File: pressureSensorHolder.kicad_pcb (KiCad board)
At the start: 2 copper layers, 65 x 61.1 mm, 12 parts, among them J1 Conn_01x04, U1 SDP8xx-ANALOG

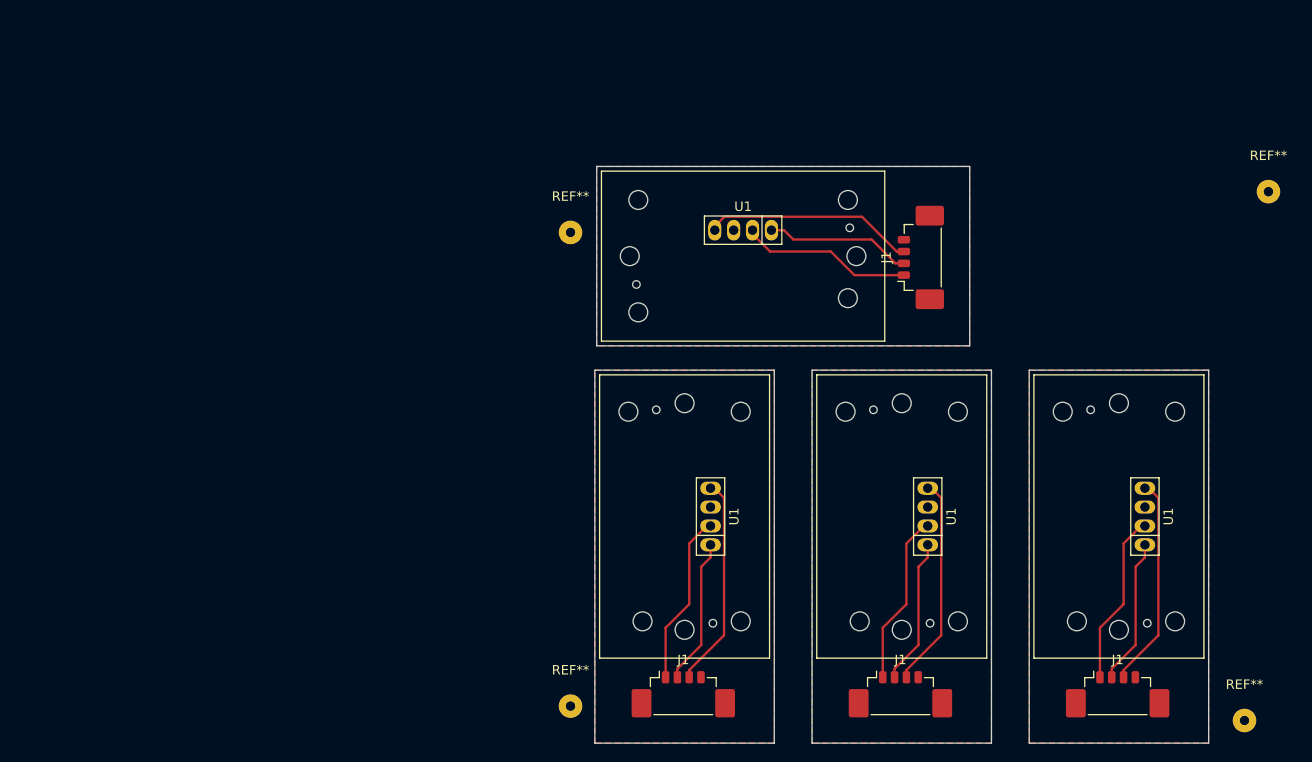
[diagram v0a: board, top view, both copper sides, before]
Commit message: Corrected sizes
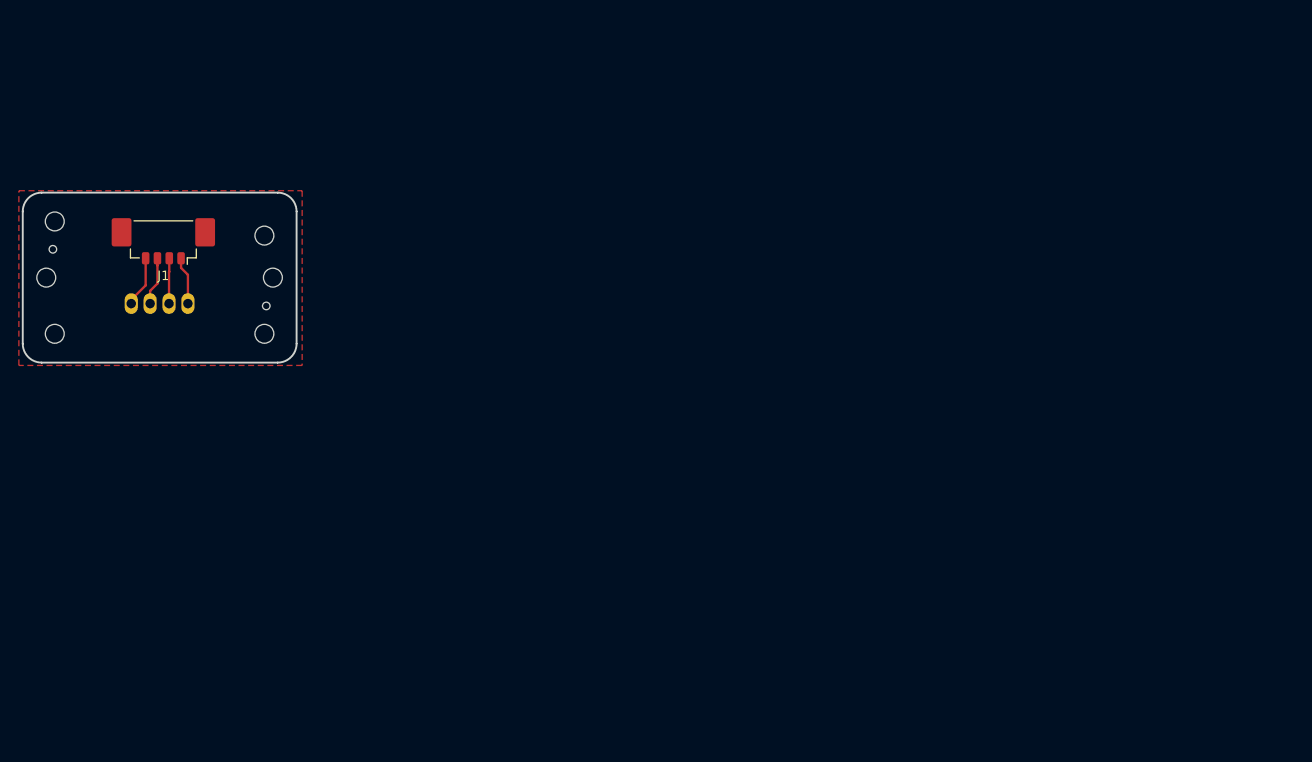
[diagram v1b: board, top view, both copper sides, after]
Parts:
- removed the J1 at (187.0, 138.9)
- removed the J1 at (164.0, 138.9)
- removed the J1 at (141.0, 138.9)
- removed REF** (x4): SolderWirePad_1x01_Drill1mm, Connector_Wire:SolderWirePad_1x01_Drill1mm
- removed the U1 at (147.3, 93.0)
- removed the U1 at (187.1, 120.6)
- removed the U1 at (164.1, 120.6)
- removed the U1 at (141.1, 120.6)
- added U1: SDP8xx-ANALOG, RESPIRECO:SDP80x, B.Cu at (85.5, 95.3)
- moved J1 79.7 mm to (85.9, 92.0), turned to 180 degrees
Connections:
- J1 pad 1: /Vdd -> /OCS_SCL
- J1 pad 2: /OCS_SCL -> /Vdd
- J1 pad 3: /AOut_SDA -> /GND
- J1 pad 4: /GND -> /AOut_SDA
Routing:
- net /AOut_SDA: track 89.5 -> 5.43 mm
- net /Vdd: track 72.9 -> 4.81 mm
- net /OCS_SCL: track 61.9 -> 5.10 mm
- net /GND: track 0.00 -> 5.12 mm
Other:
- board size 65 x 61.1 mm -> 29 x 18 mm

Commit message: New JST(PH) connection and mounting holes
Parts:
- added C1: C, Capacitor_SMD:C_1206_3216Metric, F.Cu at (148.7, 84.1)
- added H1: MountingHole, MountingHole:MountingHole_3.2mm_M3_Pad_Via, F.Cu at (134.9, 73.2)
- added H2: MountingHole, MountingHole:MountingHole_3.2mm_M3_Pad_Via, F.Cu at (134.9, 94.2)
- added JP1: SolderJumper_3_Open, Jumper:SolderJumper-3_P2.0mm_Open_TrianglePad1.0x1.5mm, F.Cu at (154.9, 80.9)
- J1: footprint Connector_Molex:Molex_PicoBlade_53398-0471_1x04-1MP_P1.25mm_Vertical -> Connector_JST:JST_PH_B4B-PH-SM4-TB_1x04-1MP_P2.00mm_Vertical; moved to B.Cu
- moved U1 64.5 mm to (148.9, 83.7), turned to 270 degrees
- moved J1 48.8 mm to (133.9, 83.7), turned to 270 degrees
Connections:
- net /GND renamed GND
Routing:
- net /Vdd: track 4.81 -> 20.6 mm, vias 0 -> 1
- net /OCS_SCL: track 5.10 -> 20.6 mm
- net /AOut_SDA: track 5.43 -> 17.2 mm
- net GND: track 5.12 -> 4.25 mm
- added copper zone on B.Cu, net GND
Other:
- board size 29 x 18 mm -> 29.5 x 31 mm
- net class Default: clearance 0.2 -> 0.254; trace_width 0.25 -> 0.254
- rule trace_clearance: 0.2 -> 0.254
- rule trace_min: 0.2 -> 0.1

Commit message: PCBWAY production files (20210110)
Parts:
- added D1: LED, LED_SMD:LED_0805_2012Metric, B.Cu at (137.7, 82.7)
- added R1: 150R, Resistor_SMD:R_0805_2012Metric, B.Cu at (137.7, 86.7)
- moved J1 1.25 mm to (132.7, 83.7)
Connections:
- C1 pad 1: /Vdd -> +3V3
- J1 pad 2: /Vdd -> +3V3
- JP1 pad : (no net) -> +3V3
- JP1 pad 1: /Vdd -> +3V3
- U1 pad 2: /Vdd -> +3V3
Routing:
- net +3V3: track 0.00 -> 29.0 mm, vias 0 -> 1
- net /Vdd: track 20.6 -> 0.00 mm, vias 1 -> 0
- net Net-(D1-Pad1): track 0.00 -> 2.15 mm
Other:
- board size 29.5 x 31 mm -> 30.5 x 31 mm
- board text added: "MoNo^^BREW lab. 20210110 artur.a.pozniak@gmail.com"

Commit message: Prod. files Lenartowice
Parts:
- C1: moved to B.Cu
- J1: value Conn_01x04 -> Conn_01x03; footprint Connector_JST:JST_PH_B4B-PH-SM4-TB_1x04-1MP_P2.00mm_Vertical -> Connector_JST:JST_PH_B3B-PH-SM4-TB_1x03-1MP_P2.00mm_Vertical
- moved C1 13.8 mm to (138.1, 75.3), turned to 90 degrees
- moved H1 2.54 mm to (132.4, 73.2)
- moved H2 2.54 mm to (132.4, 94.2)
- moved J1 0.86 mm to (133.5, 83.4)
- moved D1 0.63 mm to (138.3, 82.7)
- moved R1 0.63 mm to (138.3, 86.7)
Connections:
- J1 pad 1: /OCS_SCL -> +3V3
- J1 pad 2: +3V3 -> /AOut_SDA
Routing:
- net /OCS_SCL: track 20.6 -> 3.35 mm
- net /AOut_SDA: track 17.2 -> 19.7 mm
- net +3V3: track 29.0 -> 26.6 mm, vias 1 -> 0
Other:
- board text added: "MoNo^^BREW lab. 20210915 r2@mbrw.cc"
- board text removed: "MoNo^^BREW lab. 20210110 artur.a.pozniak@gmail.com"
